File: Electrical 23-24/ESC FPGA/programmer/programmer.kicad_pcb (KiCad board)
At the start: 2 copper layers, 73.3 x 13.9 mm, 44 parts, among them J201 USB_B_Micro, J202 SFH11-PBPC-D07-ST-BK, J203 Conn_01x05_Pin, J204 Conn_01x11_Pin, J205 Conn_01x14_Pin, SW201 SW_DPST, U201 93C46C, U202 NUP2202, U203 AMS1117-3.3, U204 FT2232HL, Y201 12MHZ

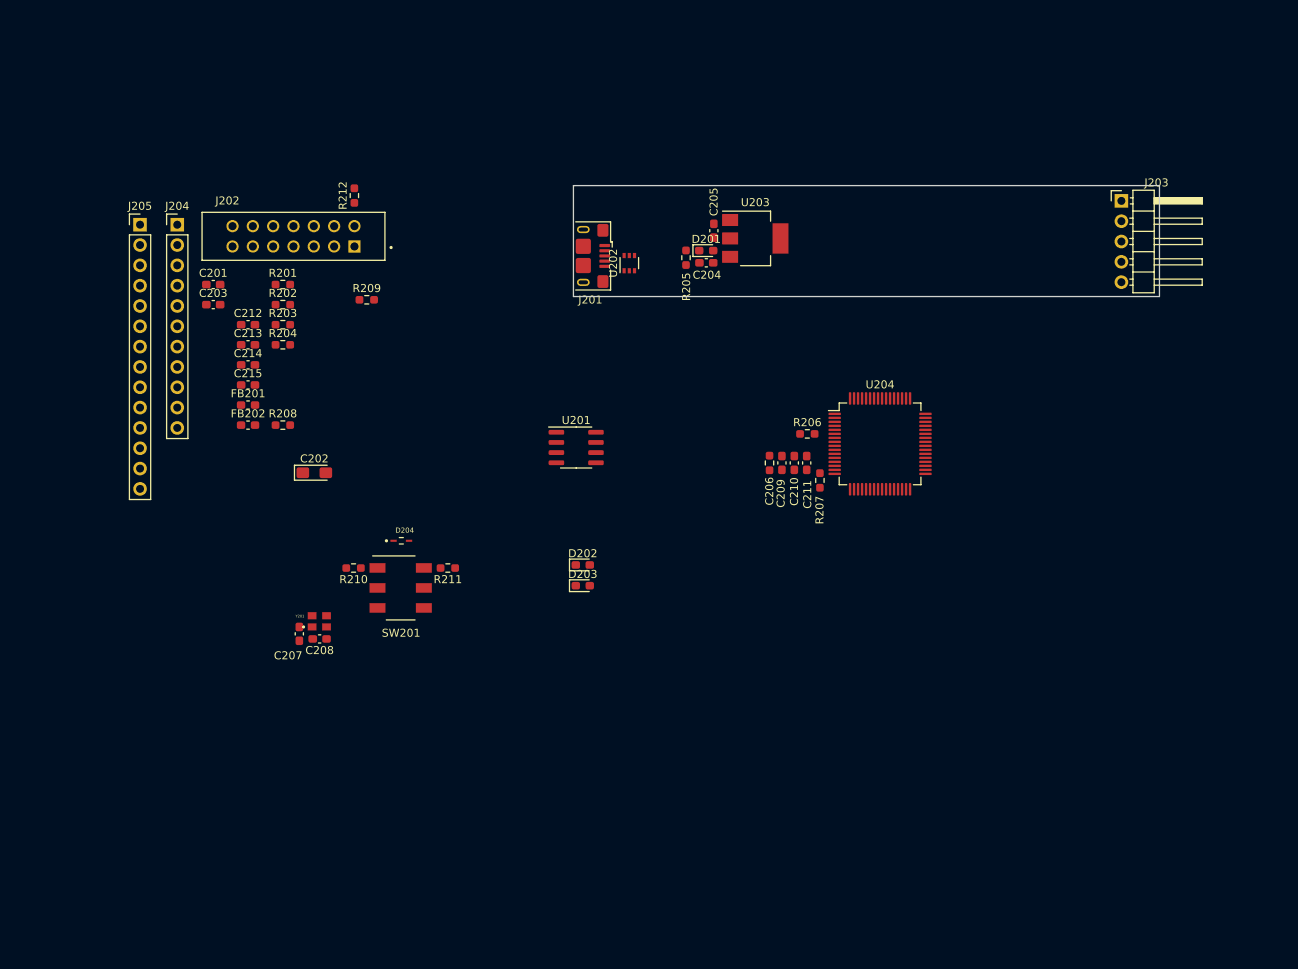
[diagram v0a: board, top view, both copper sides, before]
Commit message: Layout almost done, need to try routing
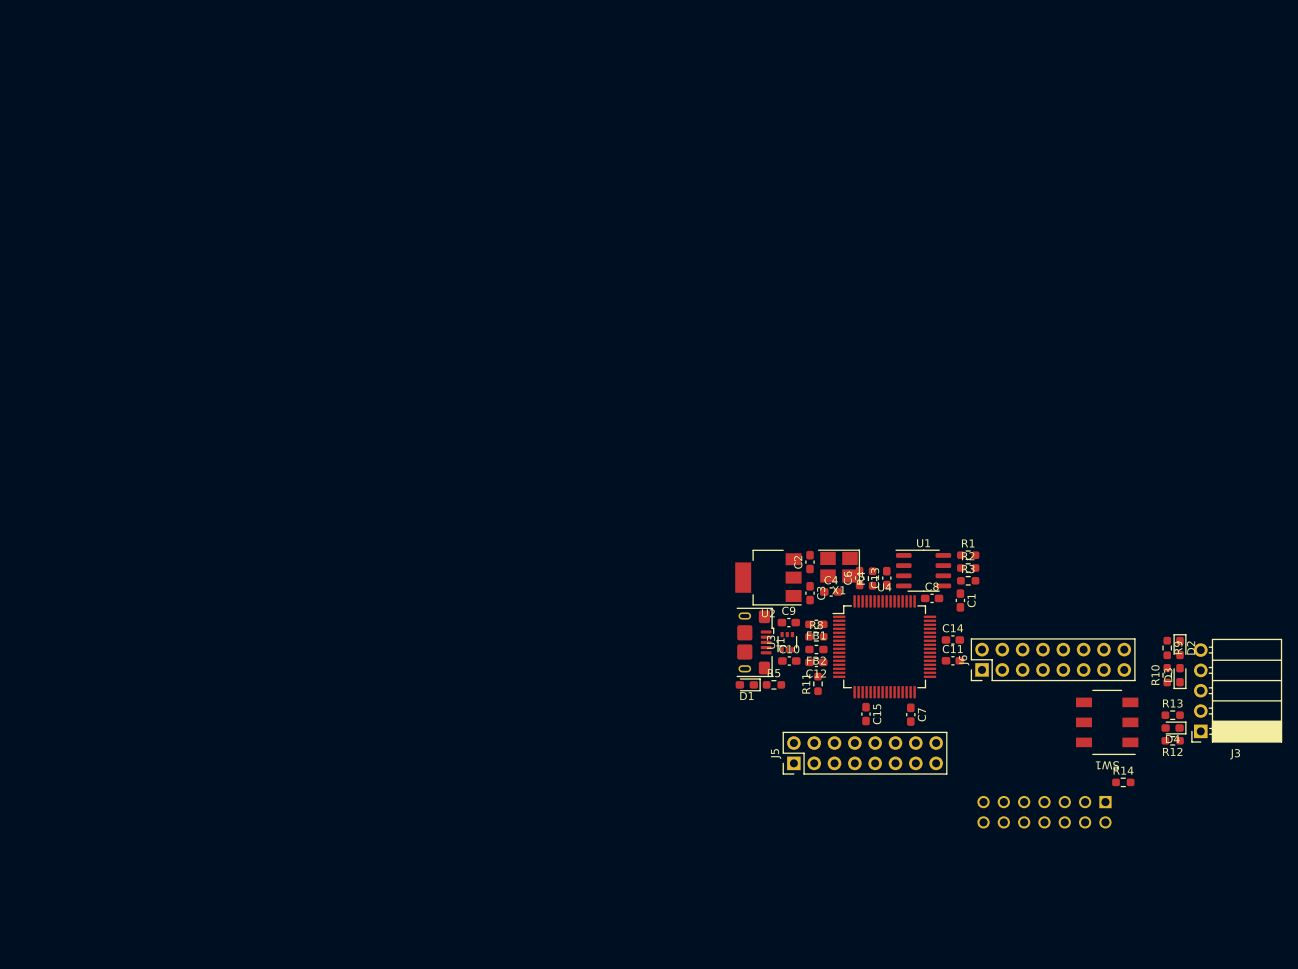
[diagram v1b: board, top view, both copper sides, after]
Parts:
- removed C201, C203, C204, C205, C209, C210, C211, C212, C213, C214, C215: 0.1uF, Capacitor_SMD:C_0603_1608Metric_Pad1.08x0.95mm_HandSolder
- removed C202: 10uF, Capacitor_Tantalum_SMD:CP_EIA-3216-18_Kemet-A_Pad1.58x1.35mm_HandSolder
- removed C206: 3.3uF, Resistor_SMD:R_0603_1608Metric_Pad0.98x0.95mm_HandSolder
- removed C207, C208: 27pF, Capacitor_SMD:C_0603_1608Metric_Pad1.08x0.95mm_HandSolder
- removed D201: pwr, LED_SMD:LED_0603_1608Metric_Pad1.05x0.95mm_HandSolder
- removed D202: RX_LED, LED_SMD:LED_0603_1608Metric_Pad1.05x0.95mm_HandSolder
- removed D203: TX_LED, LED_SMD:LED_0603_1608Metric_Pad1.05x0.95mm_HandSolder
- removed D204: D_Schottky, programmer:DIOM168X70N
- removed FB201, FB202: BLM18KG121TN1D, Inductor_SMD:L_0603_1608Metric_Pad1.05x0.95mm_HandSolder
- removed J201: USB_B_Micro, Connector_USB:USB_Micro-B_Amphenol_10118193-0001LF_Horizontal
- removed J202: SFH11-PBPC-D07-ST-BK, programmer:SULLINS_SFH11-PBPC-D07-ST-BK
- removed J203: Conn_01x05_Pin, Connector_PinHeader_2.54mm:PinHeader_1x05_P2.54mm_Horizontal
- removed J204: Conn_01x11_Pin, Connector_PinHeader_2.54mm:PinHeader_1x11_P2.54mm_Vertical
- removed J205: Conn_01x14_Pin, Connector_PinHeader_2.54mm:PinHeader_1x14_P2.54mm_Vertical
- removed R201, R202, R203: 10K, Resistor_SMD:R_0603_1608Metric_Pad0.98x0.95mm_HandSolder
- removed R204: 2.2K, Resistor_SMD:R_0603_1608Metric_Pad0.98x0.95mm_HandSolder
- removed R205, R208, R209: 220, Resistor_SMD:R_0603_1608Metric_Pad0.98x0.95mm_HandSolder
- removed R206: 12K, Resistor_SMD:R_0603_1608Metric_Pad0.98x0.95mm_HandSolder
- removed R207: 1K, Resistor_SMD:R_0603_1608Metric_Pad0.98x0.95mm_HandSolder
- removed R210, R211: 470, Resistor_SMD:R_0603_1608Metric_Pad0.98x0.95mm_HandSolder
- removed R212: 0, Resistor_SMD:R_0603_1608Metric_Pad0.98x0.95mm_HandSolder
- removed SW201: SW_DPST, programmer:DPDT
- removed U201: 93C46C, Package_SO:SOIC-8_3.9x4.9mm_P1.27mm
- removed U202: NUP2202, Package_TO_SOT_SMD:SOT-363_SC-70-6
- removed U203: AMS1117-3.3, Package_TO_SOT_SMD:SOT-223-3_TabPin2
- removed U204: FT2232HL, Package_QFP:LQFP-64_10x10mm_P0.5mm
- removed Y201: 12MHZ, programmer:OSC_ECS-2033-120-BN
- added C1: 0.1uF, Capacitor_SMD:C_0603_1608Metric_Pad1.08x0.95mm_HandSolder, F.Cu at (159.8, 97.9)
- added C10: 10uF, Capacitor_SMD:C_0603_1608Metric_Pad1.08x0.95mm_HandSolder, F.Cu at (138.4, 105.4)
- added C11: 0.1uF, Capacitor_SMD:C_0603_1608Metric_Pad1.08x0.95mm_HandSolder, F.Cu at (158.8, 105.4)
- added C12: 0.1uF, Capacitor_SMD:C_0603_1608Metric_Pad1.08x0.95mm_HandSolder, F.Cu at (141.8, 105.6)
- added C13: 0.1uF, Capacitor_SMD:C_0603_1608Metric_Pad1.08x0.95mm_HandSolder, F.Cu at (150.6, 95.1)
- added C14: 0.1uF, Capacitor_SMD:C_0603_1608Metric_Pad1.08x0.95mm_HandSolder, F.Cu at (158.8, 102.8)
- added C15: 0.1uF, Capacitor_SMD:C_0603_1608Metric_Pad1.08x0.95mm_HandSolder, F.Cu at (147.9, 112.1)
- added C2: 0.1uF, Capacitor_SMD:C_0603_1608Metric_Pad1.08x0.95mm_HandSolder, F.Cu at (140.9, 93.1)
- added C3: 0.1uF, Capacitor_SMD:C_0603_1608Metric_Pad1.08x0.95mm_HandSolder, F.Cu at (141.0, 96.9)
- added C4: 0.01uF, Capacitor_SMD:C_0603_1608Metric_Pad1.08x0.95mm_HandSolder, F.Cu at (143.6, 96.8)
- added C6: 0.1uF, Capacitor_SMD:C_0603_1608Metric_Pad1.08x0.95mm_HandSolder, F.Cu at (147.2, 95.1)
- added C7: 0.1uF, Capacitor_SMD:C_0603_1608Metric_Pad1.08x0.95mm_HandSolder, F.Cu at (153.6, 112.1)
- added C8: 3.3uF, Capacitor_SMD:C_0603_1608Metric_Pad1.08x0.95mm_HandSolder, F.Cu at (156.2, 97.6)
- added C9: 0.1uF, Capacitor_SMD:C_0603_1608Metric_Pad1.08x0.95mm_HandSolder, F.Cu at (138.3, 100.6)
- added D1: pwr, LED_SMD:LED_0603_1608Metric_Pad1.05x0.95mm_HandSolder, F.Cu at (133.1, 108.4)
- added D2: RX_LED, LED_SMD:LED_0603_1608Metric_Pad1.05x0.95mm_HandSolder, F.Cu at (187.2, 103.8)
- added D3: TX_LED, LED_SMD:LED_0603_1608Metric_Pad1.05x0.95mm_HandSolder, F.Cu at (187.2, 107.2)
- added D4: D_Schottky, Diode_SMD:D_0603_1608Metric_Pad1.05x0.95mm_HandSolder, F.Cu at (186.3, 113.8)
- added FB1: BLM18KG121TN1D, Inductor_SMD:L_0603_1608Metric_Pad1.05x0.95mm_HandSolder, F.Cu at (141.7, 100.8)
- added FB2: BLM18KG121TN1D, Inductor_SMD:L_0603_1608Metric_Pad1.05x0.95mm_HandSolder, F.Cu at (141.8, 104.0)
- added J1: USB_B_Micro, Connector_USB:USB_Micro-B_Amphenol_10118193-0001LF_Horizontal, F.Cu at (132.8, 103.1)
- added J2: SFH11-PBPC-D07-ST-BK, programmer:SULLINS_SFH11-PBPC-D07-ST-BK, B.Cu at (170.3, 124.3)
- added J3: Conn_01x05_Pin, Connector_PinSocket_2.54mm:PinSocket_1x05_P2.54mm_Horizontal, F.Cu at (189.8, 114.2)
- added J5: Conn_02x8_Pin, Connector_PinHeader_2.54mm:PinHeader_2x08_P2.54mm_Vertical, F.Cu at (138.9, 118.2)
- added J6: Conn_02x8_Pin, Connector_PinHeader_2.54mm:PinHeader_2x08_P2.54mm_Vertical, F.Cu at (162.5, 106.5)
- added R1: 10K, Resistor_SMD:R_0603_1608Metric_Pad0.98x0.95mm_HandSolder, F.Cu at (160.7, 92.2)
- added R10: 220, Resistor_SMD:R_0603_1608Metric_Pad0.98x0.95mm_HandSolder, F.Cu at (185.6, 107.2)
- added R11: 1K, Resistor_SMD:R_0603_1608Metric_Pad0.98x0.95mm_HandSolder, F.Cu at (141.9, 108.3)
- added R12: 470, Resistor_SMD:R_0603_1608Metric_Pad0.98x0.95mm_HandSolder, F.Cu at (186.3, 115.4)
- added R13: 470, Resistor_SMD:R_0603_1608Metric_Pad0.98x0.95mm_HandSolder, F.Cu at (186.3, 112.2)
- added R14: 0, Resistor_SMD:R_0603_1608Metric_Pad0.98x0.95mm_HandSolder, F.Cu at (180.1, 120.6)
- added R2: 10K, Resistor_SMD:R_0603_1608Metric_Pad0.98x0.95mm_HandSolder, F.Cu at (160.7, 93.8)
- added R3: 10K, Resistor_SMD:R_0603_1608Metric_Pad0.98x0.95mm_HandSolder, F.Cu at (160.7, 95.4)
- added R4: 2.2K, Resistor_SMD:R_0603_1608Metric_Pad0.98x0.95mm_HandSolder, F.Cu at (148.8, 95.1)
- added R5: 220, Resistor_SMD:R_0603_1608Metric_Pad0.98x0.95mm_HandSolder, F.Cu at (136.4, 108.4)
- added R8: 12K, Resistor_SMD:R_0603_1608Metric_Pad0.98x0.95mm_HandSolder, F.Cu at (141.8, 102.4)
- added R9: 220, Resistor_SMD:R_0603_1608Metric_Pad0.98x0.95mm_HandSolder, F.Cu at (185.6, 103.8)
- added SW1: SW_DPST, programmer:DPDT, F.Cu at (178.1, 113.1)
- added U1: 93C46C, Package_SO:SOIC-8_3.9x4.9mm_P1.27mm, F.Cu at (155.2, 94.1)
- added U2: AMS1117-3.3, Package_TO_SOT_SMD:SOT-223, F.Cu at (135.8, 95.0)
- added U3: NUP2202, Package_TO_SOT_SMD:SOT-363_SC-70-6, F.Cu at (138.1, 103.1)
- added U4: FT2232HL, Package_QFP:LQFP-64_10x10mm_P0.5mm, F.Cu at (150.3, 103.7)
- added X1: ISM92-3351AH-12.000MHZ, Oscillator:Oscillator_SMD_Abracon_ASE-4Pin_3.2x2.5mm_HandSoldering, F.Cu at (144.6, 93.7)
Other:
- board outline removed

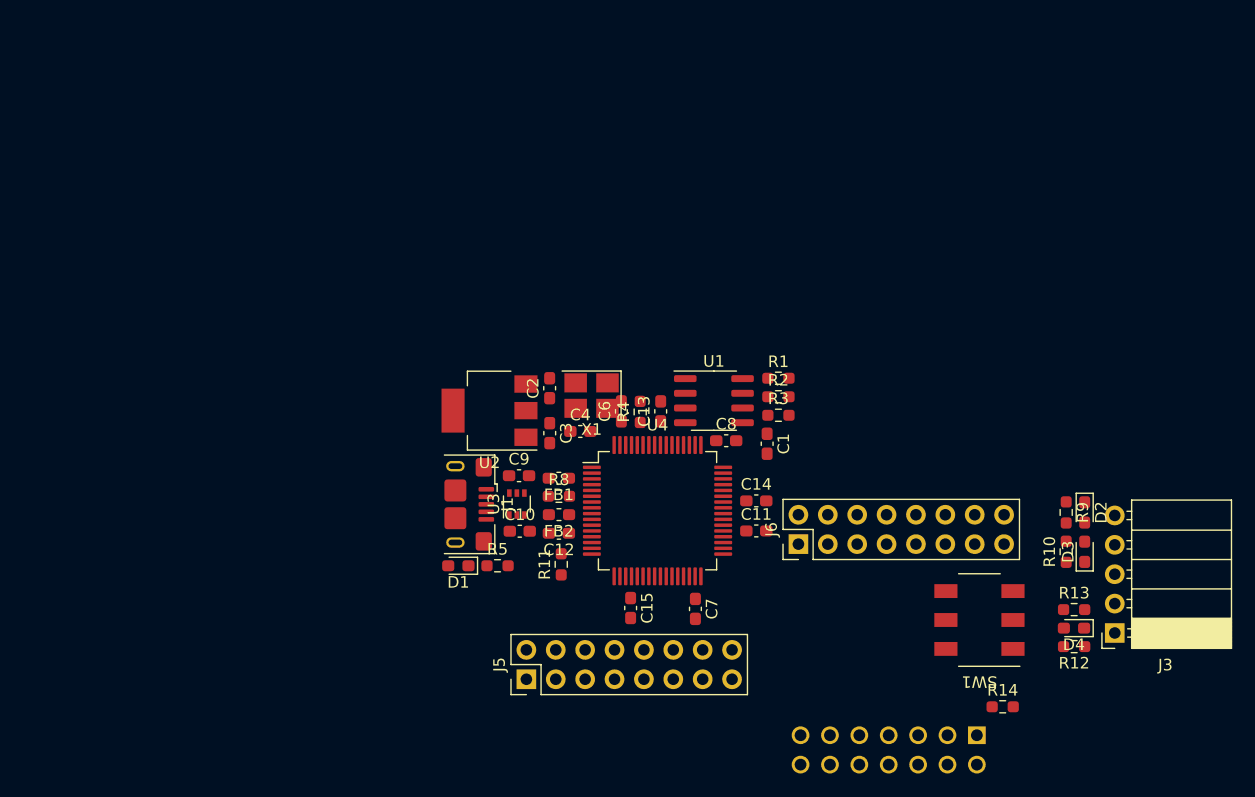
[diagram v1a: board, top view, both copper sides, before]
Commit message: Finished the core, connecting ports
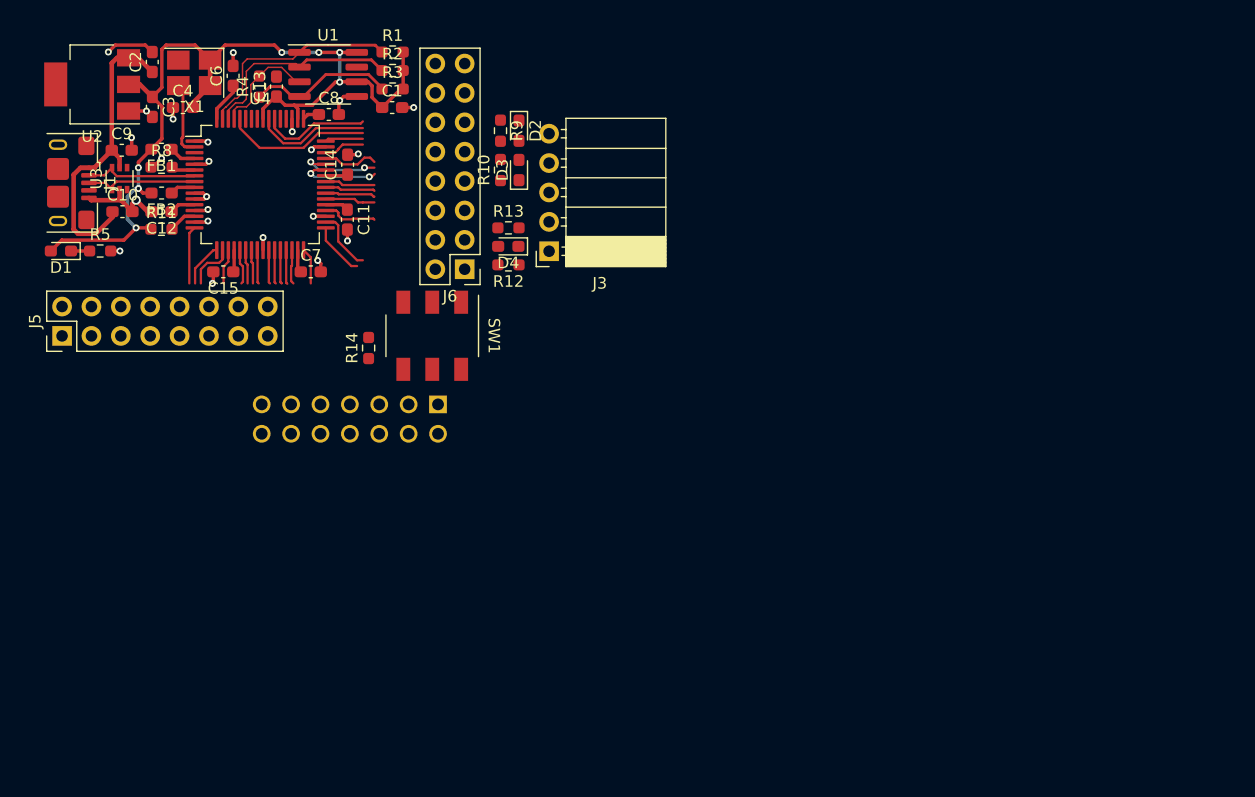
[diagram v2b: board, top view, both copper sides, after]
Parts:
- moved R14 63.0 mm to (125.3, 89.6), turned to 90 degrees
- moved D4 59.0 mm to (137.4, 80.8)
- moved J3 59.0 mm to (140.9, 81.2)
- moved R10 59.0 mm to (136.7, 74.2)
- moved R12 59.0 mm to (137.4, 82.4)
- moved R13 59.0 mm to (137.4, 79.2)
- moved R9 59.0 mm to (136.7, 70.8)
- moved D2 59.0 mm to (138.3, 70.8)
- moved D3 59.0 mm to (138.3, 74.2)
- moved J2 54.7 mm to (123.7, 95.7)
- moved SW1 53.3 mm to (130.8, 88.5), turned to -90 degrees
- moved J5 49.9 mm to (98.8, 88.5)
- moved C14 45.7 mm to (123.5, 73.7), turned to 90 degrees
- moved C15 45.7 mm to (112.7, 83.0), turned to 180 degrees
- moved R11 45.1 mm to (107.4, 79.3), turned to 0 degrees
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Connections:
- U3 pad 1: Net-(J1-D-) -> Net-(J1-D+)
- U3 pad 6: Net-(J1-D+) -> Net-(J1-D-)
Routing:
- net +3.3V: track 0.00 -> 83.8 mm, vias 0 -> 7
- net GND: track 0.00 -> 39.8 mm, vias 0 -> 23
- net +5V: track 0.00 -> 27.0 mm
- net Net-(U1-CS): track 0.00 -> 18.6 mm
- net Net-(U1-SCLK): track 0.00 -> 17.9 mm
- net Net-(U1-DO): track 0.00 -> 12.7 mm
- net /prog/PWREN: track 0.00 -> 12.7 mm
- net Net-(U4-BCBUS4): track 0.00 -> 10.1 mm
- net Net-(J1-D-): track 0.00 -> 9.91 mm
- net Net-(J1-D+): track 0.00 -> 9.83 mm
- net Net-(U4-BCBUS3): track 0.00 -> 9.42 mm
- net Net-(U1-DI): track 0.00 -> 9.37 mm
- net +1V8: track 0.00 -> 9.19 mm
- net /prog/DSR: track 0.00 -> 7.25 mm, vias 0 -> 2
- net /prog/DTR: track 0.00 -> 7.19 mm, vias 0 -> 2
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
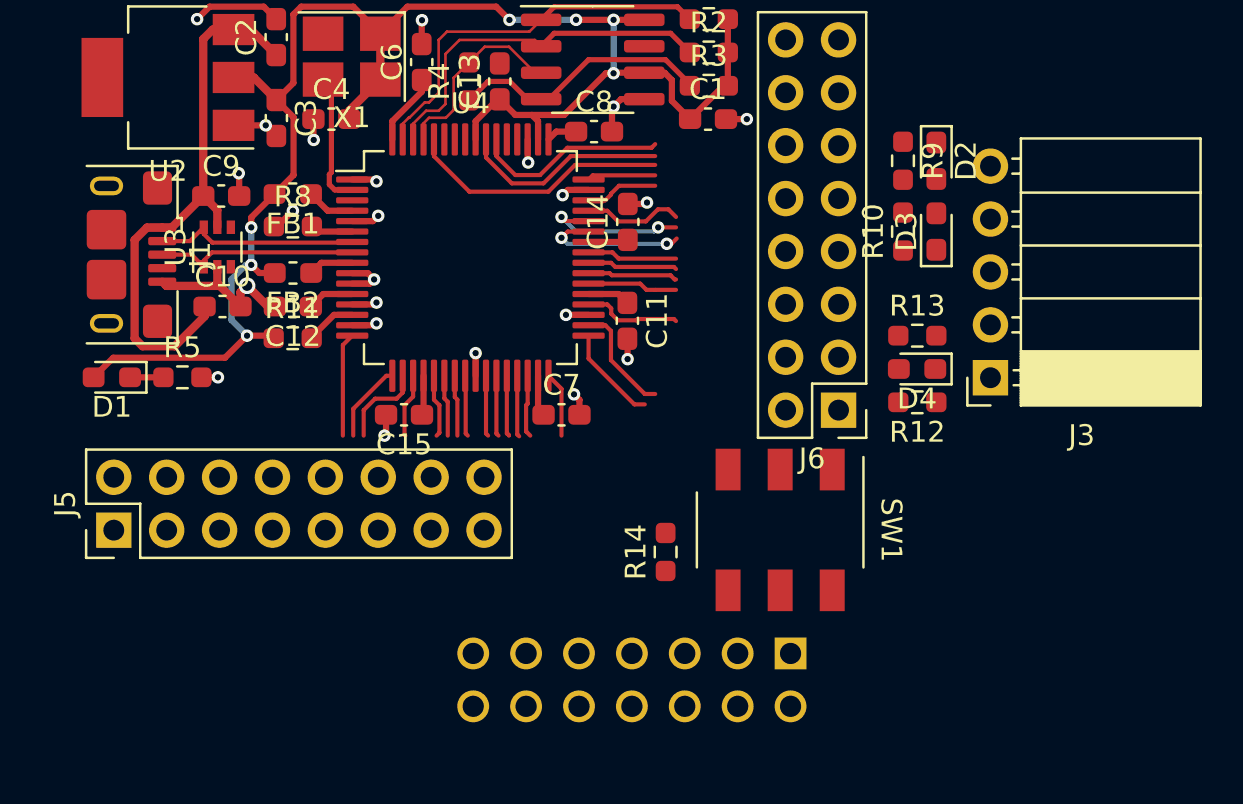
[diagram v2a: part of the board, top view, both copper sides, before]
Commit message: Finished length matched traces
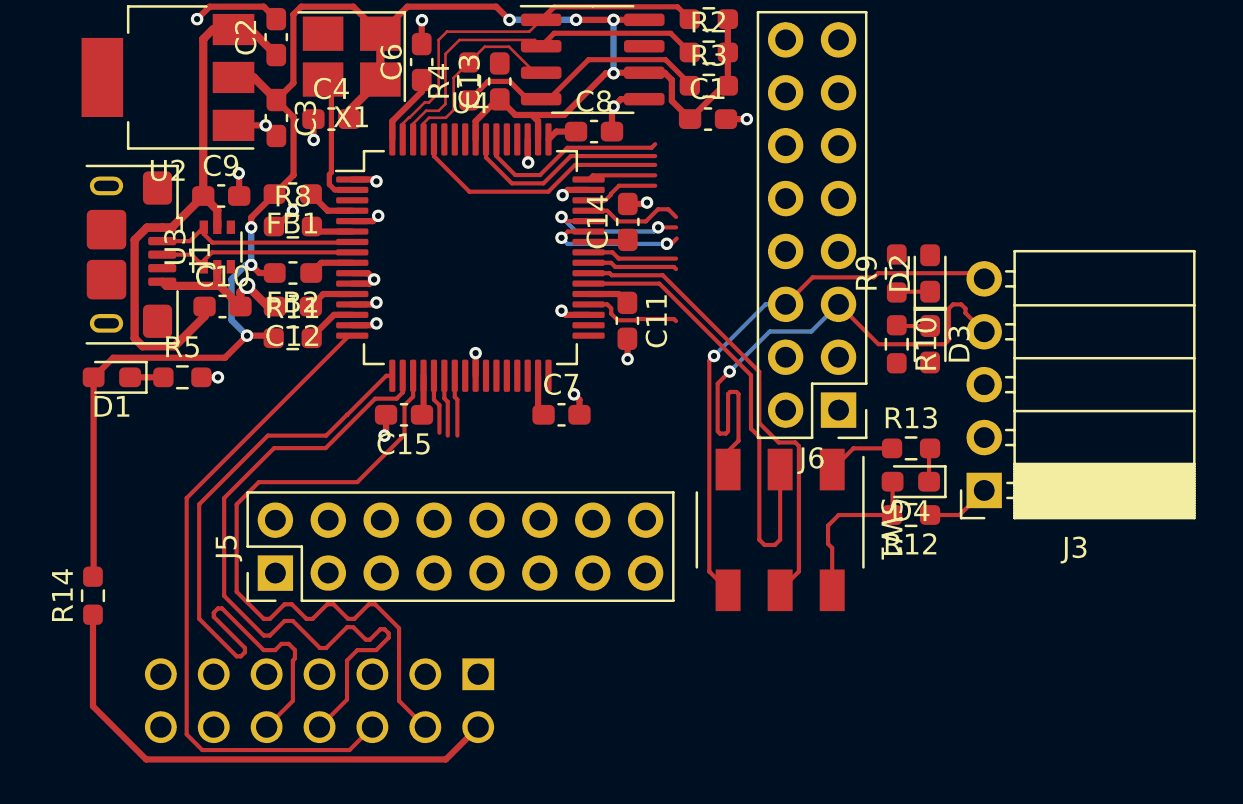
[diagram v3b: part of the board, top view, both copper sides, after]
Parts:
- moved R14 27.6 mm to (97.8, 91.7)
- moved J2 15.0 mm to (108.7, 96.7)
- moved J5 8.03 mm to (106.6, 90.6)
- moved D2 5.42 mm to (138.0, 76.2), turned to 90 degrees
- moved D4 5.42 mm to (137.1, 86.2)
- moved R9 5.42 mm to (136.4, 76.2), turned to 90 degrees
- moved D3 5.42 mm to (138.0, 79.6), turned to -90 degrees
- moved J3 5.42 mm to (140.6, 86.6)
- moved R10 5.42 mm to (136.4, 79.6), turned to -90 degrees
- moved R12 5.42 mm to (137.1, 87.8)
- moved R13 5.42 mm to (137.1, 84.6)
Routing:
- net /prog/TMS: track 3.06 -> 32.2 mm
- net /prog/TDO: track 4.25 -> 33.1 mm
- net /prog/TDI: track 3.82 -> 32.2 mm
- net /prog/TCK: track 4.99 -> 32.2 mm
- net /prog/UART_TX: track 0.00 -> 26.5 mm, vias 0 -> 1
- net /prog/UART_RX: track 0.00 -> 26.5 mm, vias 0 -> 1
- net Net-(J2-Pad2): track 0.00 -> 24.6 mm
- net /prog/RX: track 4.32 -> 22.3 mm
- net /prog/TX: track 4.32 -> 22.3 mm
- net +3.3V: track 83.8 -> 93.4 mm
- net Net-(D4-A): track 0.00 -> 8.08 mm
- net /prog/H7: track 5.39 -> 0.00 mm
- net /prog/H6: track 4.71 -> 0.00 mm
- net Net-(R13-Pad1): track 0.00 -> 3.30 mm
- net /prog/H5: track 3.13 -> 0.00 mm
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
